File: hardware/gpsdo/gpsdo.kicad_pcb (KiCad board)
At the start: 4 copper layers, 70 x 70 mm, 86 parts, among them J1 Conn_01x02, J2 Conn_02x03_Top_Bottom, J3 USB_C_Receptacle_USB2.0_14P, J4 Conn_01x03, J5 Conn_Coaxial, U1 74HC4040D_652, U2 74HC4040D_652, U3 REF5040AD, U4 AD5541A, U5 OPA197xD, U6 STM32F411CEUx, U7 AMS1117-3.3, U9 SN74LVC1G125DBV, X1 X322516MLB4SI

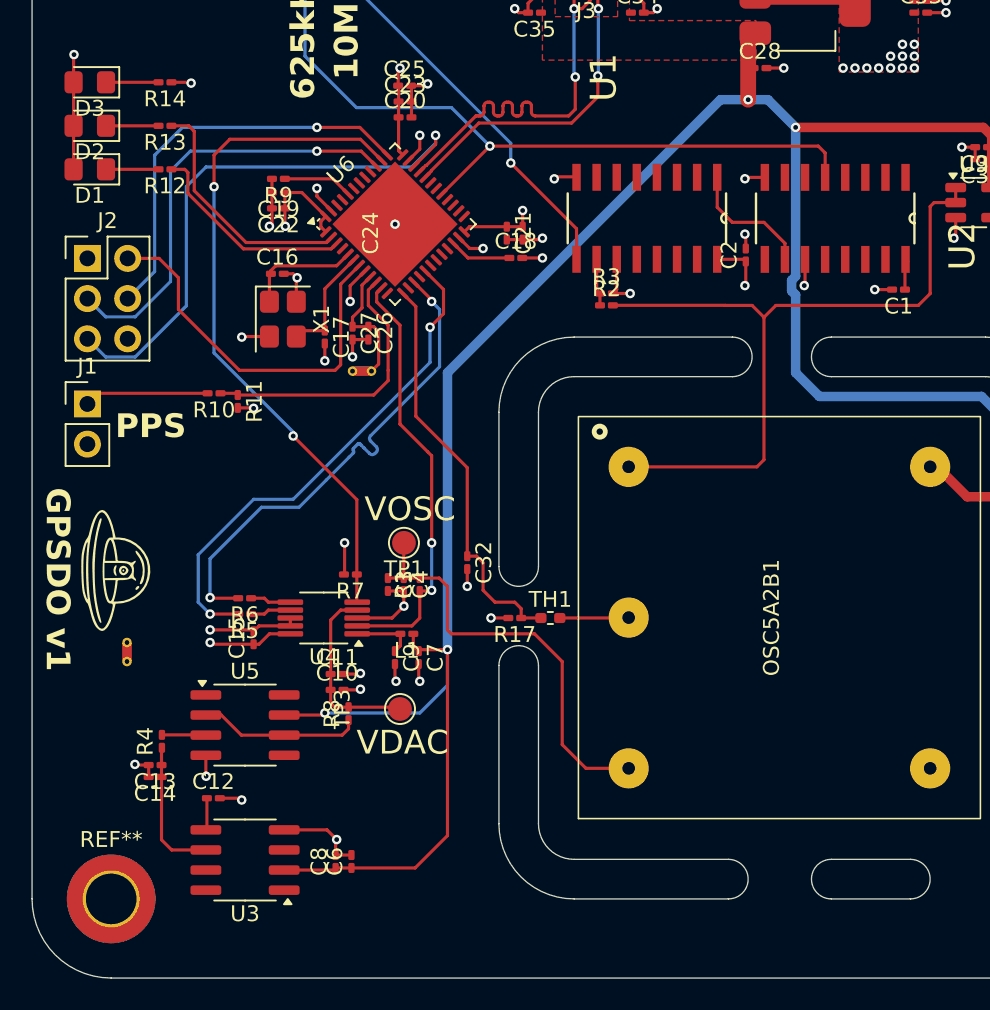
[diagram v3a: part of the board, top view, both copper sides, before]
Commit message: add symbols to pcb
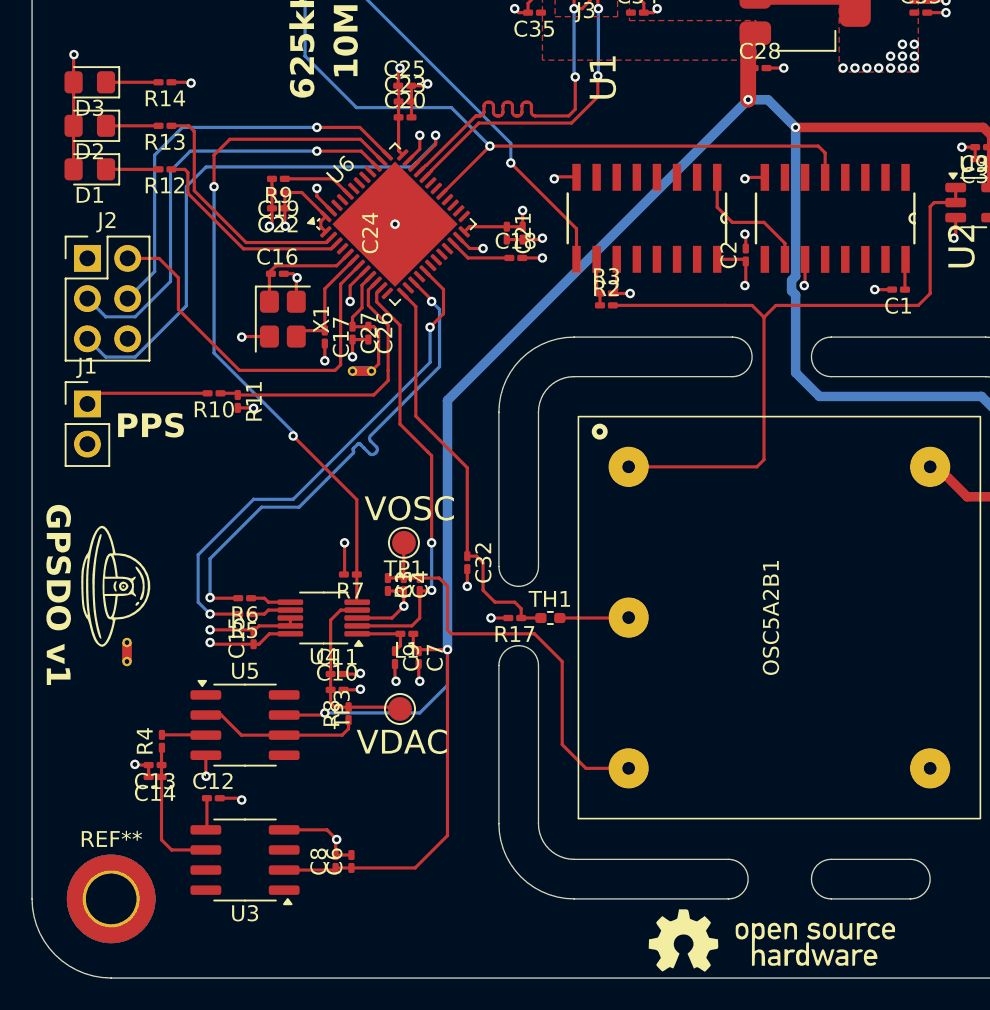
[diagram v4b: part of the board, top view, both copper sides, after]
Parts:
- added G***: LOGO, LOGO, F.Cu at (154.5, 132.5)
- moved G*** 1.00 mm to (113.0, 110.0)
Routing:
- net VCC_5V: track 159.5 -> 158.5 mm
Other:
- board text added: "Made with love in MUC"

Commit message: cleanup pcb
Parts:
- moved R17 0.25 mm to (138.2, 111.8)
- moved TH1 0.25 mm to (140.5, 111.8)
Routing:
- net GND: track 56.1 -> 54.3 mm
- net VCC_5V: track 158.5 -> 157.0 mm
- net OSC_OUT: track 7.96 -> 6.66 mm
- net VDD_3V3: track 45.4 -> 44.3 mm
- net PPS_5V: track 7.91 -> 6.92 mm
- net OSC_IN: track 7.88 -> 7.19 mm

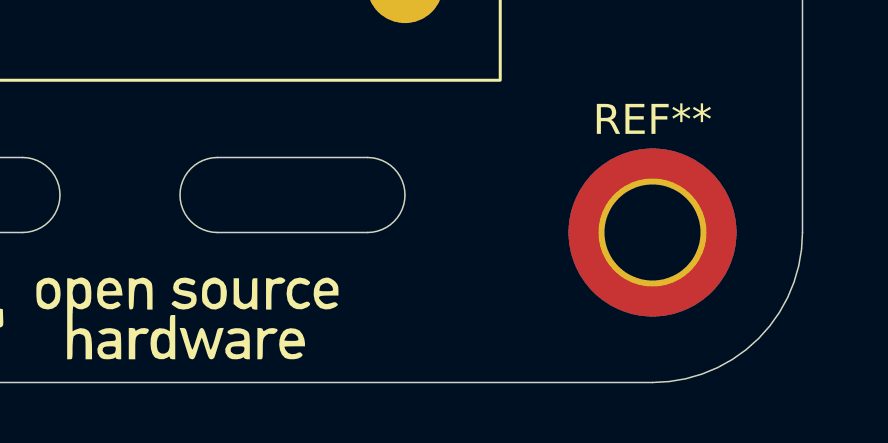
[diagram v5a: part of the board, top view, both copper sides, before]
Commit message: add qr code
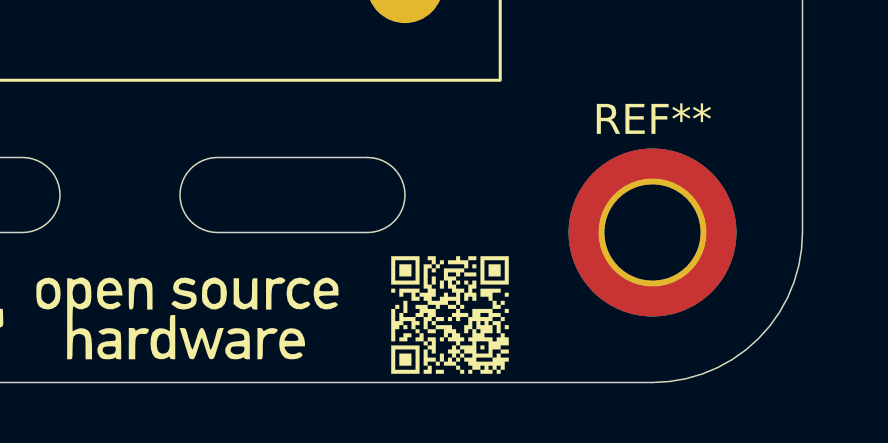
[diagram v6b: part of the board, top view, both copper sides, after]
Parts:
- added G***: LOGO, LOGO, F.Cu at (166.0, 132.5)

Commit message: bugfixing and fine tuning
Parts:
- moved C1 0.75 mm to (161.8, 91.2)
- moved OSC5A2B1 0.22 mm to (155.0, 111.8)
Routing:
- net GNDA: track 38.3 -> 44.0 mm
- net USB_P: track 25.7 -> 22.6 mm
- net VDD_3V3: track 44.3 -> 46.1 mm, vias 32 -> 33
- net NRST: track 24.5 -> 23.3 mm
- net GND: track 54.3 -> 54.8 mm

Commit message: cleanup
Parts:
- moved C3 13.8 mm to (140.8, 118.8), turned to 180 degrees
- moved C4 13.8 mm to (140.8, 119.8), turned to 180 degrees
- moved TP1 4.03 mm to (133.2, 110.8)
- moved C5 3.51 mm to (169.0, 101.2), turned to 0 degrees
- moved C2 3.27 mm to (150.7, 91.5), turned to 180 degrees
- moved R1 2.74 mm to (131.4, 112.5), turned to 0 degrees
- moved C1 0.79 mm to (162.5, 91.5)
- moved C10 0.52 mm to (127.0, 116.0)
- moved C11 0.52 mm to (127.0, 115.0)
- moved TP3 0.50 mm to (131.5, 117.8)
- moved L1 0.25 mm to (131.4, 113.2)
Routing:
- net Net-(OSC5A2B1-Vref): track 26.8 -> 22.5 mm
- net OCXO_Vref: track 27.3 -> 24.8 mm, vias 2 -> 0
- net GNDA: track 44.0 -> 42.3 mm, vias 15 -> 18
- net VCC_5V: track 157.1 -> 156.7 mm, vias 5 -> 4
